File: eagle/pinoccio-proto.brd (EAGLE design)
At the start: 25.4 x 43.2 mm, 3 parts

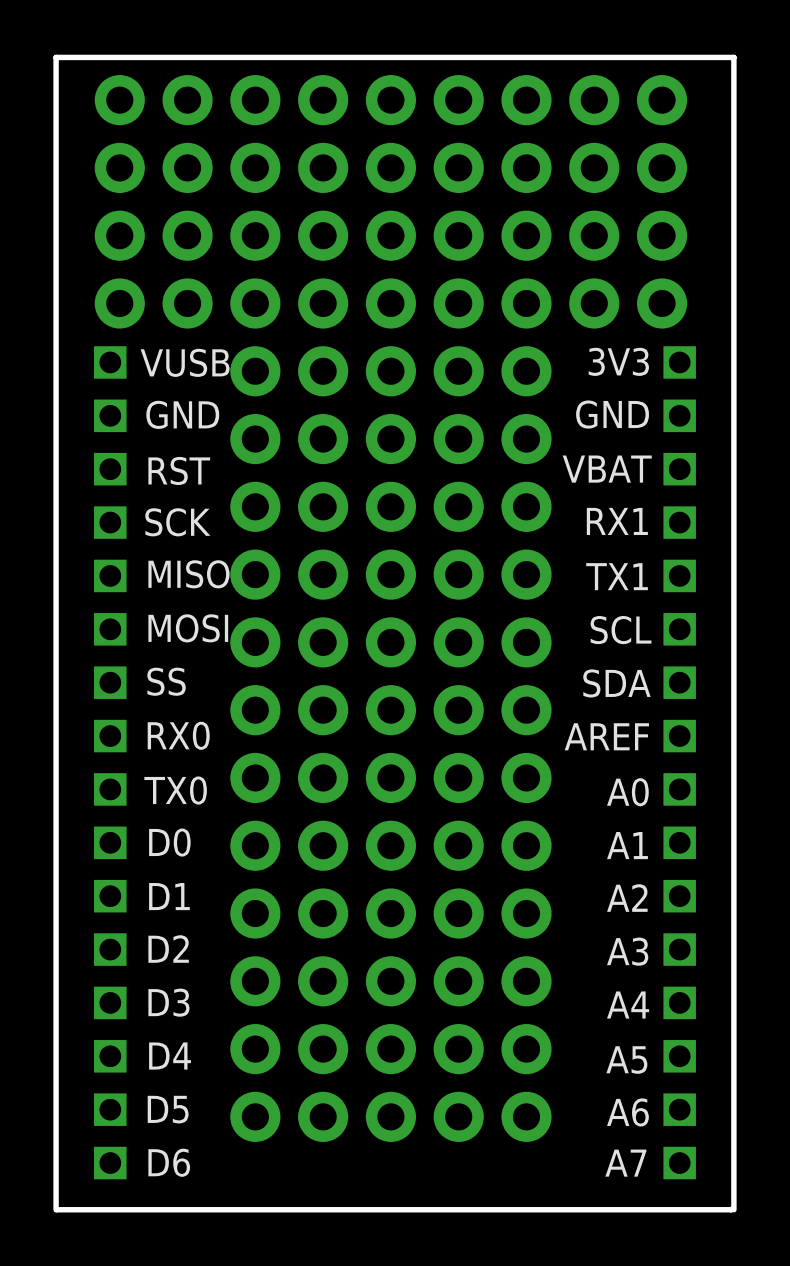
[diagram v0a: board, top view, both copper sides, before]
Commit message: Break out ground and power buses to pins
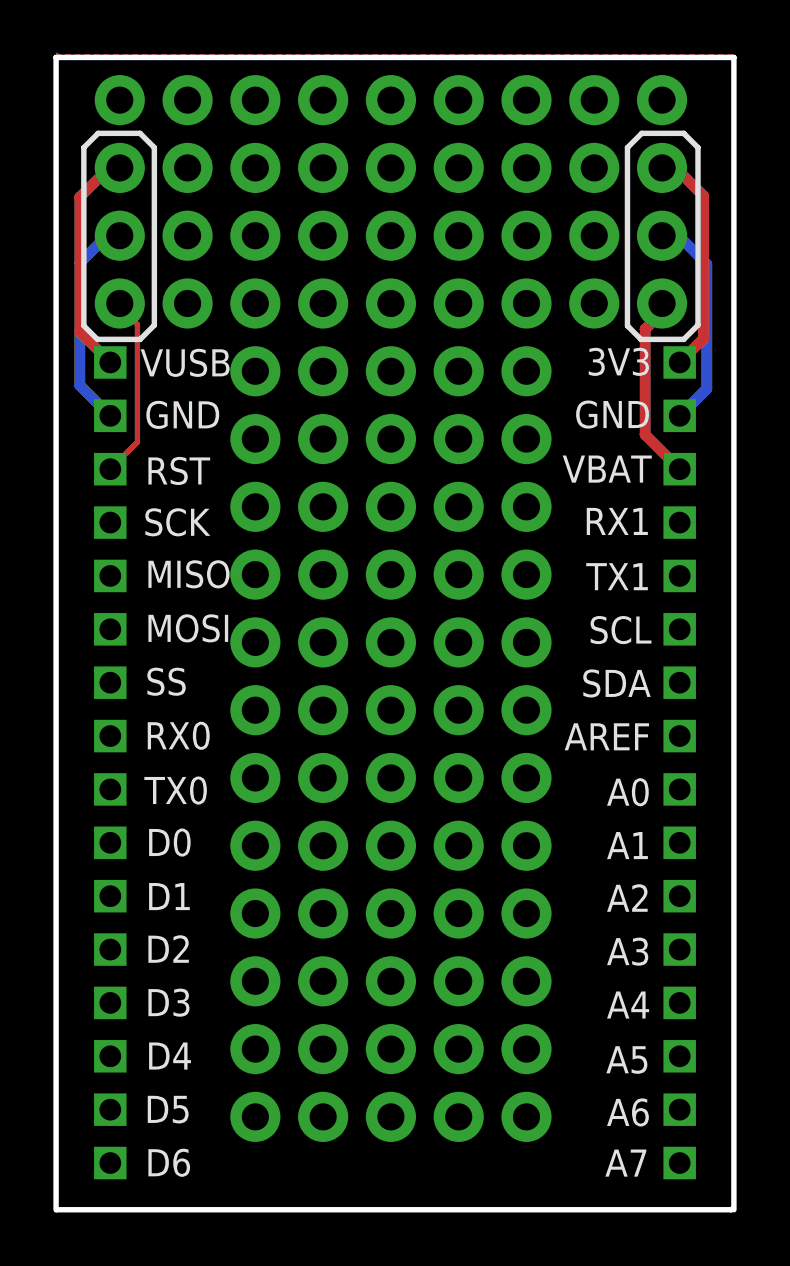
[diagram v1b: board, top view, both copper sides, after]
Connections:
- net GND: now also U$1.53, U$1.77, U$1.P-GND, U$1.P-GND2
- net RESET: now also U$1.P-RESET
- net VBAT-AE: now also U$1.P-VBAT
- net VCC-AE: now also U$1.P-VCC
- net VUSB: now also U$1.P-VUSB
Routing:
- net GND: track 0.00 -> 16.3 mm
- net VUSB: track 0.00 -> 8.62 mm
- net VCC-AE: track 0.00 -> 8.60 mm
- net VBAT-AE: track 0.00 -> 7.01 mm
- net RESET: track 0.00 -> 6.90 mm
- added copper zone on layer 1, net GND
- added copper zone on layer 16, net GND
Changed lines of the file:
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@@
 <layer number="39" name="tKeepout" color="4" fill="11" visible="no" active="yes"/>
 <layer number="40" name="bKeepout" color="1" fill="11" visible="no" active="yes"/>
-<layer number="41" name="tRestrict" color="4" fill="10" visible="yes" active="yes"/>
+<layer number="41" name="tRestrict" color="4" fill="10" visible="no" active="yes"/>
 <layer number="42" name="bRestrict" color="1" fill="10" visible="no" active="yes"/>
 <layer number="43" name="vRestrict" color="2" fill="10" visible="no" active="yes"/>
@@
 <wire x1="0.0254" y1="7.62" x2="25.2984" y2="7.62" width="0.2032" layer="20"/>
 <wire x1="25.2984" y1="7.62" x2="25.3238" y2="7.6454" width="0.2032" layer="20"/>
+<wire x1="1.5748" y1="47.9552" x2="3.1496" y2="47.9552" width="0.2032" layer="21"/>
+<wire x1="3.1496" y1="47.9552" x2="3.683" y2="47.4218" width="0.2032" layer="21"/>
+<wire x1="3.683" y1="47.4218" x2="3.683" y2="40.767" width="0.2032" layer="21"/>
+<wire x1="3.683" y1="40.767" x2="3.1496" y2="40.2336" width="0.2032" layer="21"/>
+<wire x1="3.1496" y1="40.2336" x2="1.5494" y2="40.2336" width="0.2032" layer="21"/>
+<wire x1="1.5494" y1="40.2336" x2="1.0414" y2="40.7416" width="0.2032" layer="21"/>
+<wire x1="1.0414" y1="40.7416" x2="1.0414" y2="47.4218" width="0.2032" layer="21"/>
+<wire x1="1.0414" y1="47.4218" x2="1.5748" y2="47.9552" width="0.2032" layer="21"/>
+<wire x1="21.9456" y1="47.9552" x2="23.5204" y2="47.9552" width="0.2032" layer="21"/>
+<wire x1="23.5204" y1="47.9552" x2="24.0538" y2="47.4218" width="0.2032" layer="21"/>
+<wire x1="24.0538" y1="47.4218" x2="24.0538" y2="40.767" width="0.2032" layer="21"/>
+<wire x1="24.0538" y1="40.767" x2="23.5204" y2="40.2336" width="0.2032" layer="21"/>
+<wire x1="23.5204" y1="40.2336" x2="21.9202" y2="40.2336" width="0.2032" layer="21"/>
+<wire x1="21.9202" y1="40.2336" x2="21.4122" y2="40.7416" width="0.2032" layer="21"/>
+<wire x1="21.4122" y1="40.7416" x2="21.4122" y2="47.4218" width="0.2032" layer="21"/>
+<wire x1="21.4122" y1="47.4218" x2="21.9456" y2="47.9552" width="0.2032" layer="21"/>
 </plain>
 <attributes>
@@
 <contactref element="JP-L" pad="P$2"/>
 <contactref element="JP-R" pad="P$2"/>
-<wire x1="2.032" y1="37.37" x2="23.368" y2="37.37" width="0" layer="19" extent="1-1"/>
+<contactref element="U$1" pad="P-GND"/>
+<contactref element="U$1" pad="P-GND2"/>
+<contactref element="U$1" pad="77"/>
+<contactref element="U$1" pad="53"/>
+<wire x1="2.032" y1="37.37" x2="0.889" y2="38.513" width="0.4064" layer="16"/>
+<wire x1="0.889" y1="38.513" x2="0.889" y2="43.1038" width="0.4064" layer="16"/>
+<wire x1="0.889" y1="43.1038" x2="1.905" y2="44.1198" width="0.4064" layer="16"/>
+<wire x1="1.905" y1="44.1198" x2="2.3876" y2="44.1198" width="0.4064" layer="16"/>
+<wire x1="23.368" y1="37.37" x2="24.384" y2="38.386" width="0.4064" layer="16"/>
+<wire x1="24.384" y1="38.386" x2="24.384" y2="43.053" width="0.4064" layer="16"/>
+<wire x1="24.384" y1="43.053" x2="23.3172" y2="44.1198" width="0.4064" layer="16"/>
+<wire x1="23.3172" y1="44.1198" x2="22.7076" y2="44.1198" width="0.4064" layer="16"/>
+<polygon width="0.4064" layer="1">
+<vertex x="0.0762" y="50.9524"/>
+<vertex x="0.0254" y="50.9524"/>
+<vertex x="0.0254" y="7.5946"/>
+<vertex x="25.3746" y="7.5946"/>
+<vertex x="25.3746" y="7.62"/>
+<vertex x="25.3746" y="50.9016"/>
+<vertex x="0.0762" y="50.9016"/>
+</polygon>
+<polygon width="0.4064" layer="16">
+<vertex x="0.0762" y="50.7746"/>
+<vertex x="0.0254" y="50.7746"/>
+<vertex x="0.0254" y="7.6454"/>
+<vertex x="24.892" y="7.62"/>
+<vertex x="25.0698" y="7.62"/>
+<vertex x="25.3746" y="7.5946"/>
+<vertex x="25.3746" y="50.8762"/>
+<vertex x="0.1016" y="50.8762"/>
+</polygon>
+<wire x1="12.5476" y1="33.9598" x2="12.5476" y2="44.1198" width="0" layer="19" extent="1-1"/>
+<wire x1="2.3876" y1="44.1198" x2="12.5476" y2="44.1198" width="0" layer="19" extent="1-1"/>
 </signal>
 <signal name="MOSI">
@@
 <signal name="VUSB">
 <contactref element="JP-L" pad="P$1"/>
+<contactref element="U$1" pad="P-VUSB"/>
+<wire x1="2.032" y1="39.37" x2="0.889" y2="40.513" width="0.4064" layer="1"/>
+<wire x1="0.889" y1="40.513" x2="0.889" y2="45.5676" width="0.4064" layer="1"/>
+<wire x1="0.889" y1="45.5676" x2="1.9812" y2="46.6598" width="0.4064" layer="1"/>
+<wire x1="1.9812" y1="46.6598" x2="2.3876" y2="46.6598" width="0.4064" layer="1"/>
 </signal>
 <signal name="VBAT-AE">
 <contactref element="JP-R" pad="P$3"/>
+<contactref element="U$1" pad="P-VBAT"/>
+<wire x1="23.368" y1="35.37" x2="22.0726" y2="36.6654" width="0.4064" layer="1"/>
+<wire x1="22.0726" y1="36.6654" x2="22.0726" y2="40.6146" width="0.4064" layer="1"/>
+<wire x1="22.0726" y1="40.6146" x2="22.7076" y2="41.2496" width="0.4064" layer="1"/>
+<wire x1="22.7076" y1="41.2496" x2="22.7076" y2="41.5798" width="0.4064" layer="1"/>
 </signal>
 <signal name="SSN">
@@
 <signal name="RESET">
 <contactref element="JP-L" pad="P$3"/>
+<contactref element="U$1" pad="P-RESET"/>
+<wire x1="2.032" y1="35.37" x2="3.048" y2="36.386" width="0.2032" layer="1"/>
+<wire x1="3.048" y1="36.386" x2="3.048" y2="40.7924" width="0.2032" layer="1"/>
+<wire x1="3.048" y1="40.7924" x2="2.3876" y2="41.4528" width="0.2032" layer="1"/>
+<wire x1="2.3876" y1="41.4528" x2="2.3876" y2="41.5798" width="0.2032" layer="1"/>
 </signal>
 <signal name="A0">
@@
 <signal name="VCC-AE">
 <contactref element="JP-R" pad="P$1"/>
+<contactref element="U$1" pad="P-VCC"/>
+<wire x1="23.368" y1="39.37" x2="24.257" y2="40.259" width="0.4064" layer="1"/>
+<wire x1="24.257" y1="40.259" x2="24.257" y2="45.6184" width="0.4064" layer="1"/>
+<wire x1="24.257" y1="45.6184" x2="23.2156" y2="46.6598" width="0.4064" layer="1"/>
+<wire x1="23.2156" y1="46.6598" x2="22.7076" y2="46.6598" width="0.4064" layer="1"/>
 </signal>
 <signal name="VIN">

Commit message: Update to v0.10, added solderable pads to bottom of board
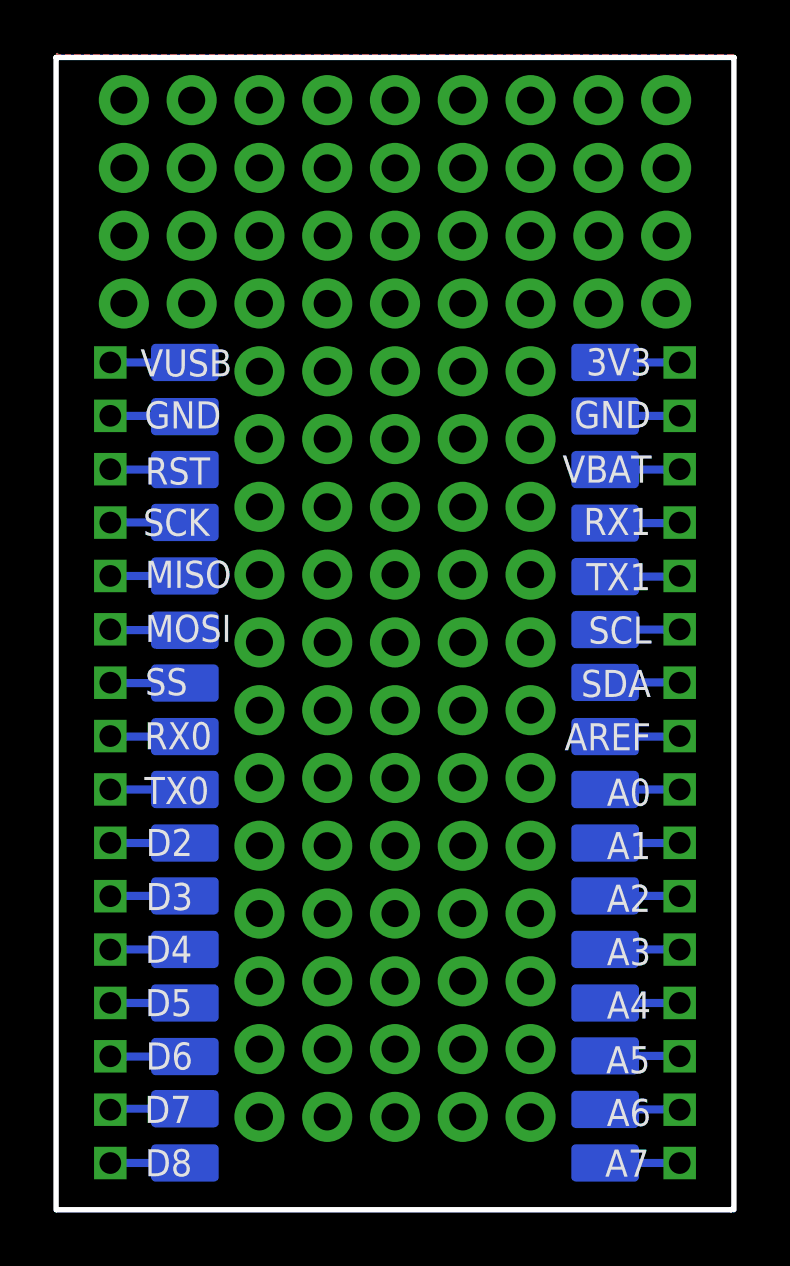
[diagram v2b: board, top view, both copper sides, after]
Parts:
- removed U$1: PROTO, Pinoccio:1X1PROTO
- added PROTOPINS: PROTO, Pinoccio:1X1PROTO
- added U$10, U$11, U$12, U$13, U$14, U$15, U$16, U$17, U$18, U$19, U$2, U$20, U$21, U$22, U$23, U$24, U$25, U$26, U$27, U$28, U$29, U$3, U$30, U$31, U$32, U$33, U$4, U$5, U$6, U$7, U$8, U$9: PAD55-RRECT, Pinoccio:PAD-100X55-RRECT
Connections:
- removed net D0: JP-L.P$10
- removed net D1: JP-L.P$11
- new net D7: JP-L.P$15, U$2.P$1
- new net D8: JP-L.P$16, U$17.P$1
- net A0: now also U$25.P$1
- net A1: now also U$24.P$1
- net A2: now also U$23.P$1
- net A3: now also U$22.P$1
- net A4: now also U$21.P$1
- net A5: now also U$20.P$1
- net A6: now also U$19.P$1
- net A7: now also U$18.P$1
- net AREF: now also U$26.P$1
- net D2: now also JP-L.P$10, U$7.P$1; no longer JP-L.P$12
- net D3: now also JP-L.P$11, U$6.P$1; no longer JP-L.P$13
- net D4: now also JP-L.P$12, U$5.P$1; no longer JP-L.P$14
- net D5: now also JP-L.P$13, U$3.P$1; no longer JP-L.P$15
- net D6: now also JP-L.P$14, U$4.P$1; no longer JP-L.P$16
- net GND: now also U$15.P$1, U$32.P$1; no longer U$1.53, U$1.77, U$1.P-GND, U$1.P-GND2
- net MISO: now also U$12.P$1
- net MOSI: now also U$11.P$1
- net RESET: now also U$14.P$1; no longer U$1.P-RESET
- net RX0: now also U$9.P$1
- net RX1: now also U$30.P$1
- net SCK: now also U$13.P$1
- net SCL: now also U$28.P$1
- net SDA: now also U$27.P$1
- net SSN: now also U$10.P$1
- net TX0: now also U$8.P$1
- net TX1: now also U$29.P$1
- net VBAT-AE: now also U$31.P$1; no longer U$1.P-VBAT
- net VCC-AE: now also U$33.P$1; no longer U$1.P-VCC
- net VUSB: now also U$16.P$1; no longer U$1.P-VUSB
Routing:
- net GND: track 16.3 -> 5.63 mm
- net VUSB: track 8.62 -> 2.79 mm
- net VCC-AE: track 8.60 -> 2.79 mm
- net VBAT-AE: track 7.01 -> 2.81 mm
- net RESET: track 6.90 -> 2.81 mm
- net D7: track 0.00 -> 2.83 mm
- net MOSI: track 0.00 -> 2.83 mm
- net TX1: track 0.00 -> 2.82 mm
- net RX0: track 0.00 -> 2.81 mm
- net AREF: track 0.00 -> 2.81 mm
- net RX1: track 0.00 -> 2.81 mm
- net A5: track 0.00 -> 2.81 mm
- net SSN: track 0.00 -> 2.81 mm
- net SDA: track 0.00 -> 2.81 mm
- net D3: track 0.00 -> 2.80 mm
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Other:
- board text added: "D7"
- board text added: "D8"
- board text added: "Pinoccio(tm) Proto v0.10"
- board text added: "Protoshield v0.10"
- board text removed: "D0"
- board text removed: "D1"
- board text removed: "Pinoccio(tm) Proto v0.9"

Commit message: version 1.0
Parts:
- moved JP-R 0.38 mm to (23.7, 39.4)
- moved JP-L 0.38 mm to (1.65, 39.4)
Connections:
- net VBAT-AE renamed VBAT
- new net BKPK-BUS: JP-L.P$2, U$15.P$1
- net GND: no longer JP-L.P$2, U$15.P$1
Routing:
- net BKPK-BUS: track 0.00 -> 3.21 mm
- net GND: track 5.63 -> 3.18 mm
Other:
- board text added: "BKPK"
- board text added: "Pinoccio(tm) Prototype Backpack v1.0"
- board text added: "Protopack v1.0"
- board text removed: "Pinoccio(tm) Proto v0.10"
- board text removed: "Protoshield v0.10"
